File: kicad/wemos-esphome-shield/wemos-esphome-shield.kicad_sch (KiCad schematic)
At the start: 19 parts, among them Q1 2N2219, Q2 2N2219, T1 Transformer_1P_1S, U1 WeMos_D1_mini

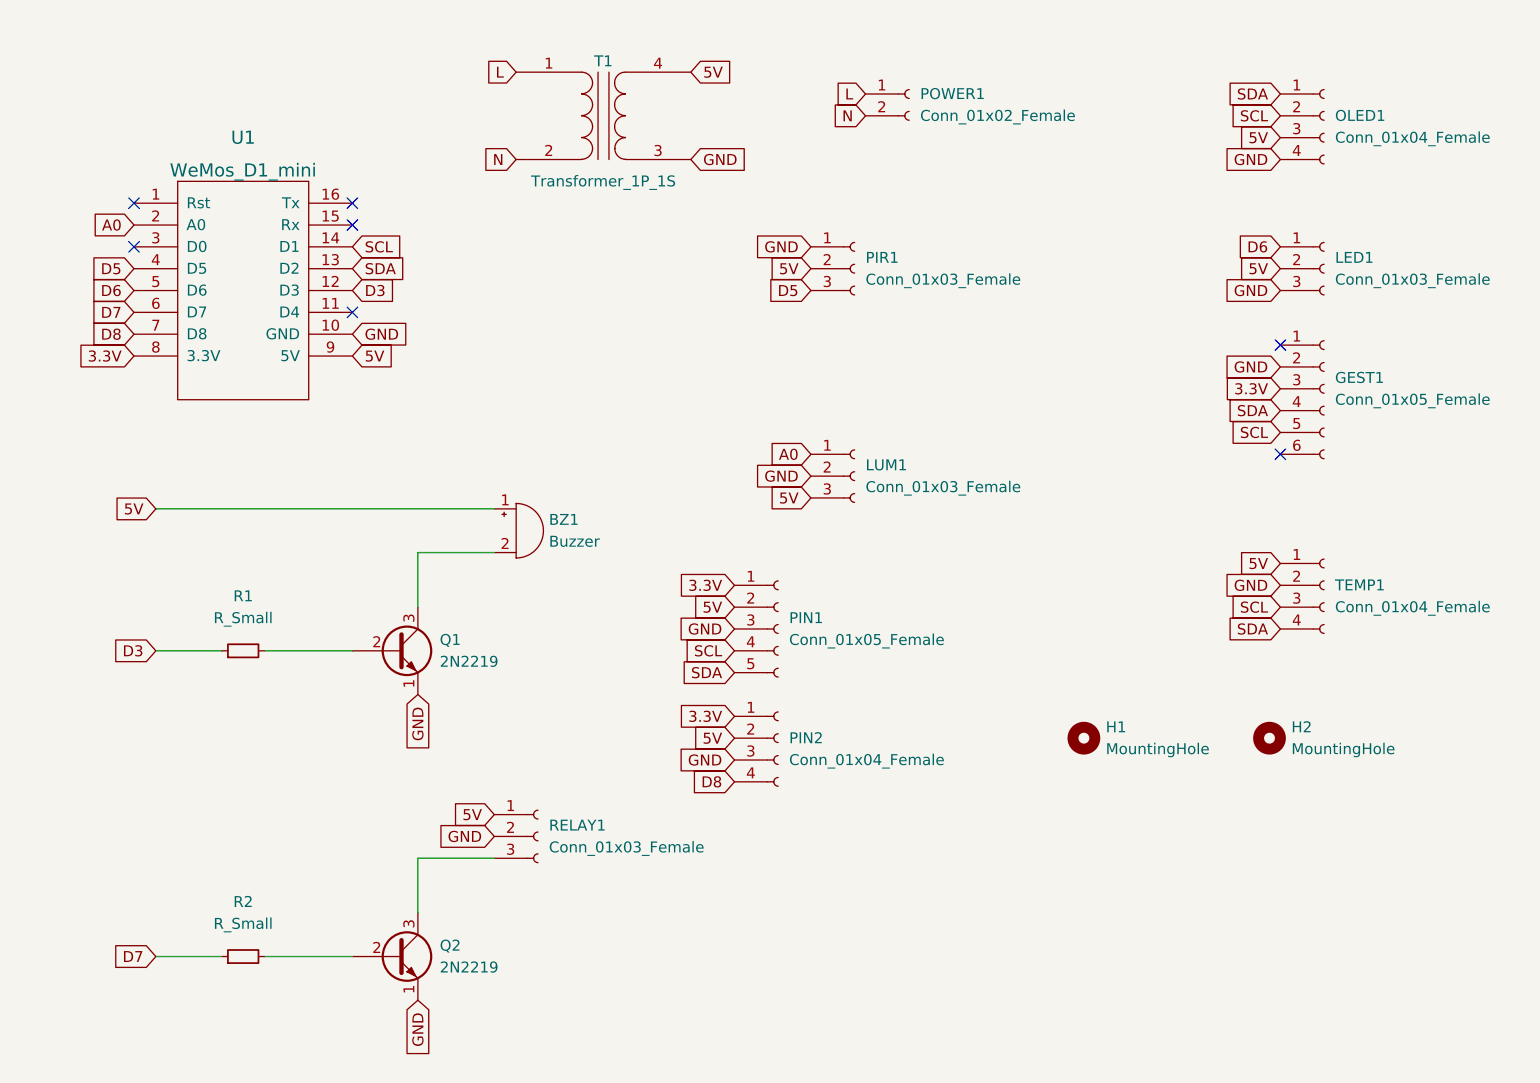
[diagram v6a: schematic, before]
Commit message: footprint fixes
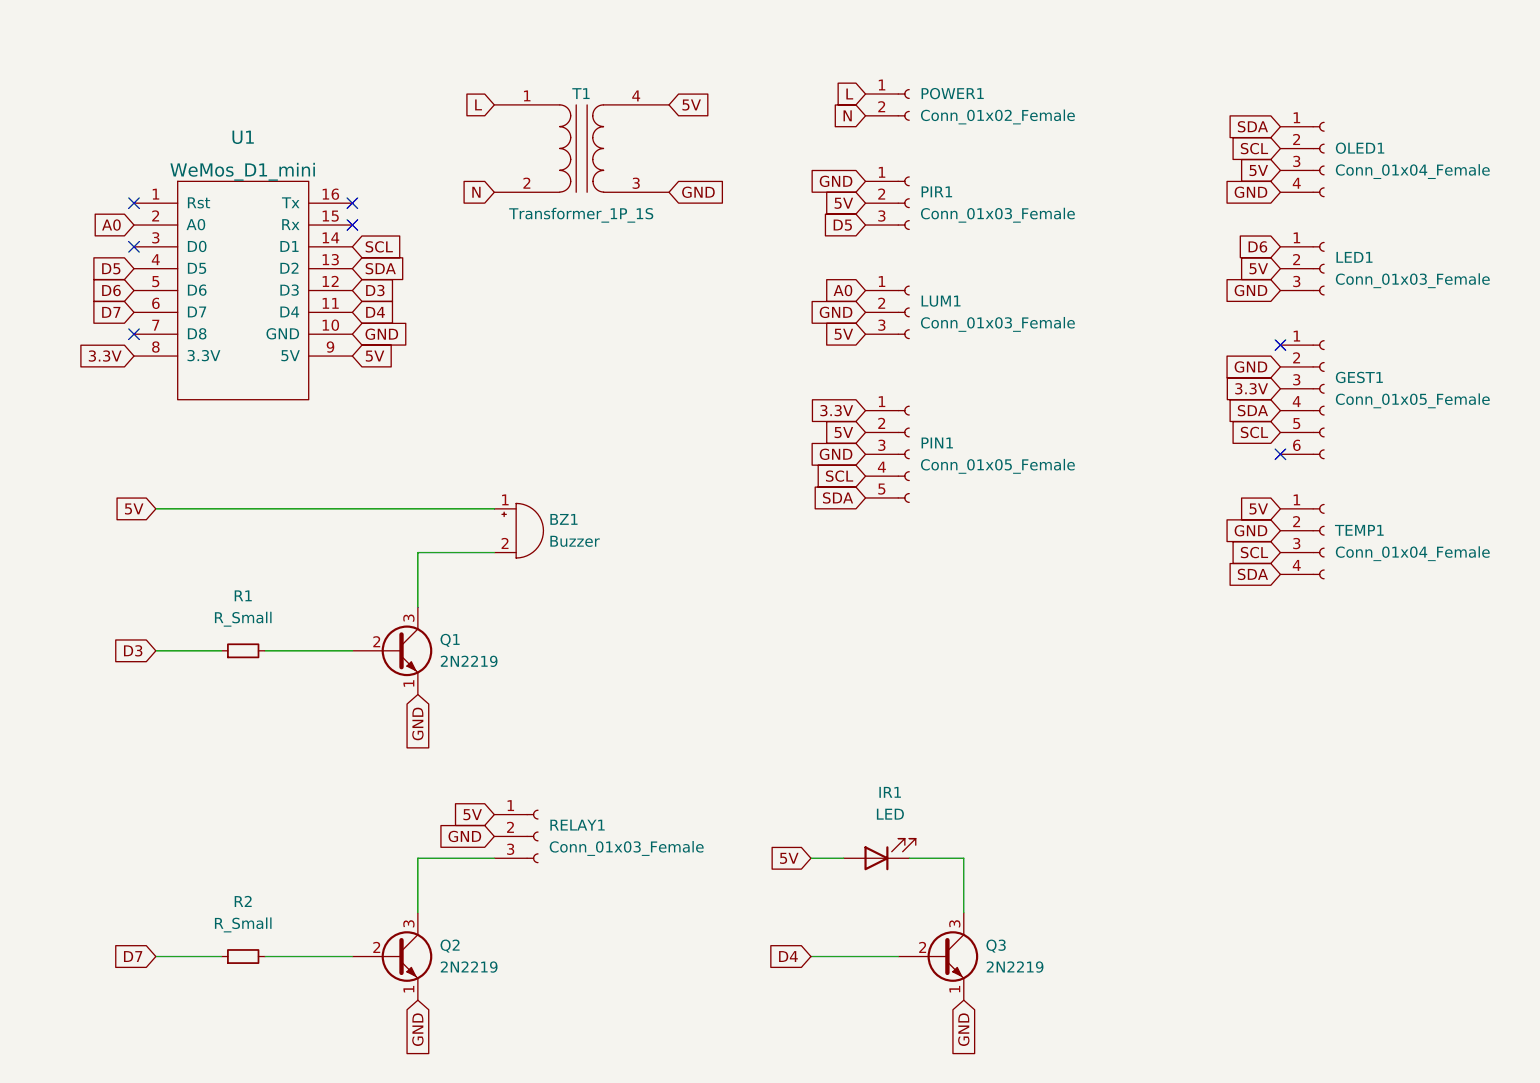
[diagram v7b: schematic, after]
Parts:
- removed H1, H2: MountingHole, MountingHole:MountingHole_3.2mm_M3, symbol Mechanical:MountingHole
- removed PIN2: Conn_01x04_Female, Connector_PinHeader_2.54mm:PinHeader_1x04_P2.54mm_Vertical, symbol Connector:Conn_01x04_Female
- added IR1: LED, LED_THT:LED_D5.0mm, symbol Device:LED
- added Q3: 2N2219, Package_TO_SOT_THT:TO-92L_Inline, symbol Transistor_BJT:2N2219
- TEMP1: footprint internal:BME280 -> Connector_JST:JST_XH_B4B-XH-AM_1x04_P2.50mm_Vertical
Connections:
- net 5V: now also IR1.2 (A)
- net GND: now also Q3.1 (E)
- net D4: now reaches U1.11 (D4)
- net D4: now also Q3.2 (B)
- net D8: no longer names the net of U1.7 (D8)
- new net: IR1.1 (K), Q3.3 (C)
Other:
- moved on the sheet: LUM1, OLED1, PIN1, PIR1, T1, TEMP1

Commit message: new footprints
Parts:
- removed GEST1: Conn_01x05_Female, internal:APDS9960, symbol Connector:Conn_01x06_Female
- removed PIR1: Conn_01x03_Female, internal:SR602, symbol Connector:Conn_01x03_Female
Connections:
- net A0: no longer U1.2 (A0)
- net RX: now reaches U1.15 (Rx)
- net TX: now reaches U1.16 (Tx)
- no-connect marks 7 -> 4
